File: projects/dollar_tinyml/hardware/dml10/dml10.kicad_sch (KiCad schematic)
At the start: 24 parts, among them J1 Conn_01x03, J2 USB_A, J3 Conn_01x04, U1 CH32V003F4P6, U2 LTC4054ES5-4.2, U3 LIS2DH, U4 LM321

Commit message: dollarml: Some notes on trees and Human Activity Detection
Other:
- note added: "CH32V003A4M6"
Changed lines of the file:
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@@
     (effects (font (size 3 3)) (justify left bottom))
+  )
+  (text "CH32V003A4M6" (at 130.175 70.485 0)
+    (effects (font (size 1.27 1.27)) (justify left bottom))
   )
   (text "Bias" (at 44.45 163.195 0)

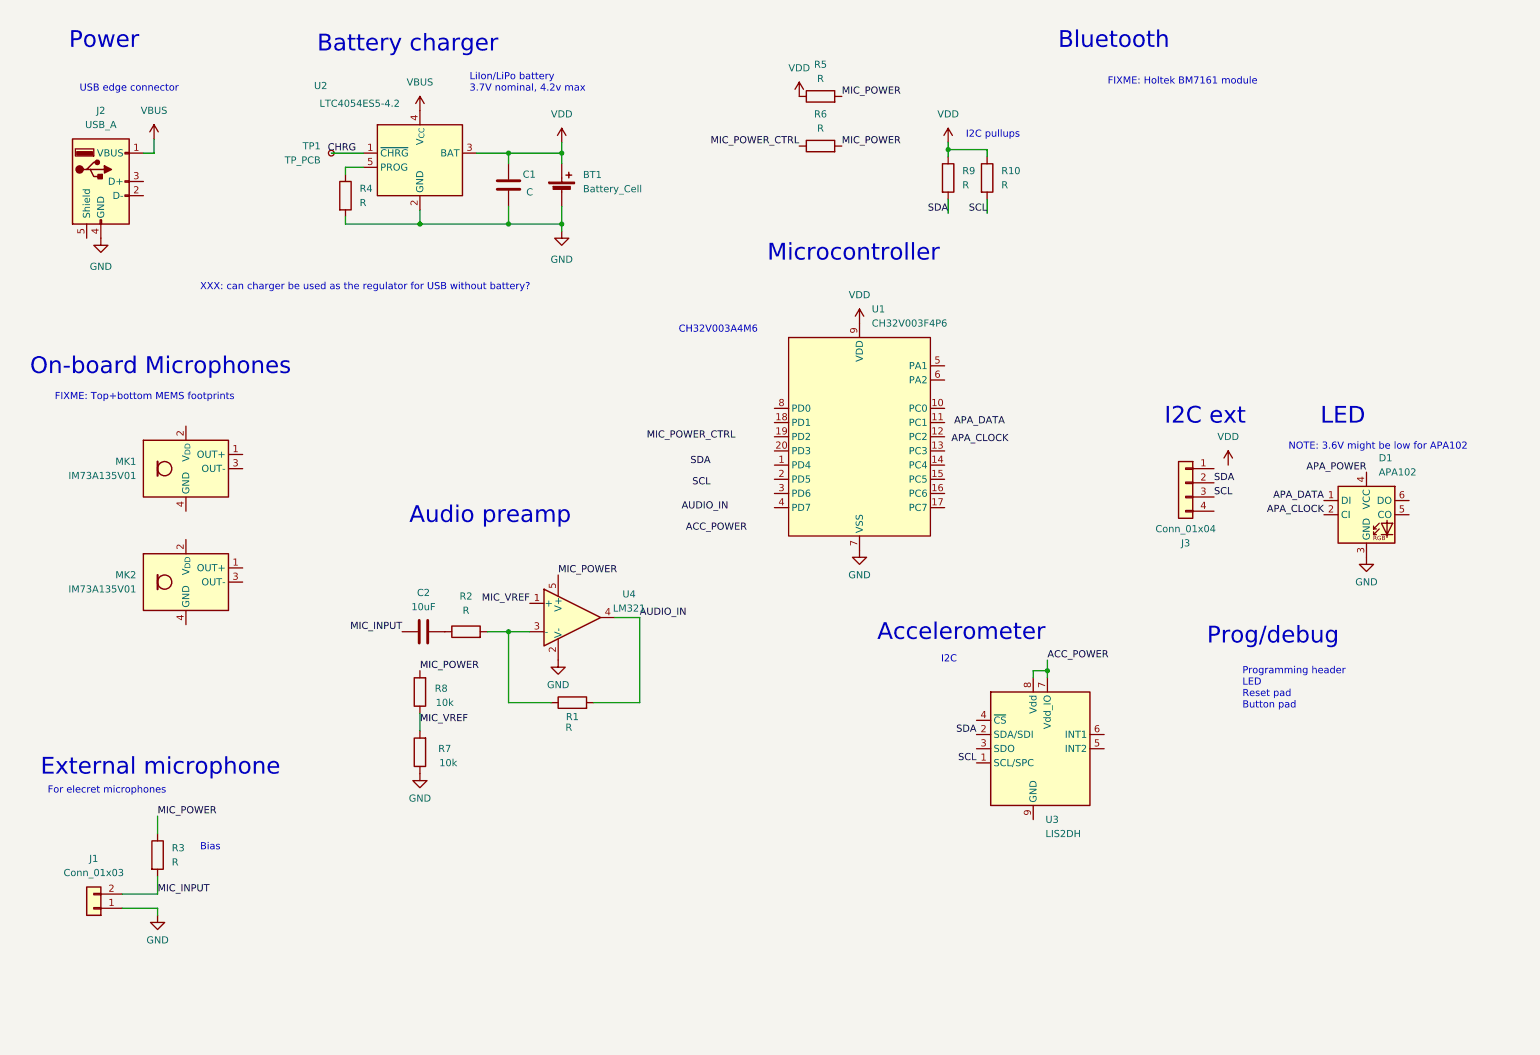
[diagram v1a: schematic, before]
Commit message: dollarml: Schematic and board sketch
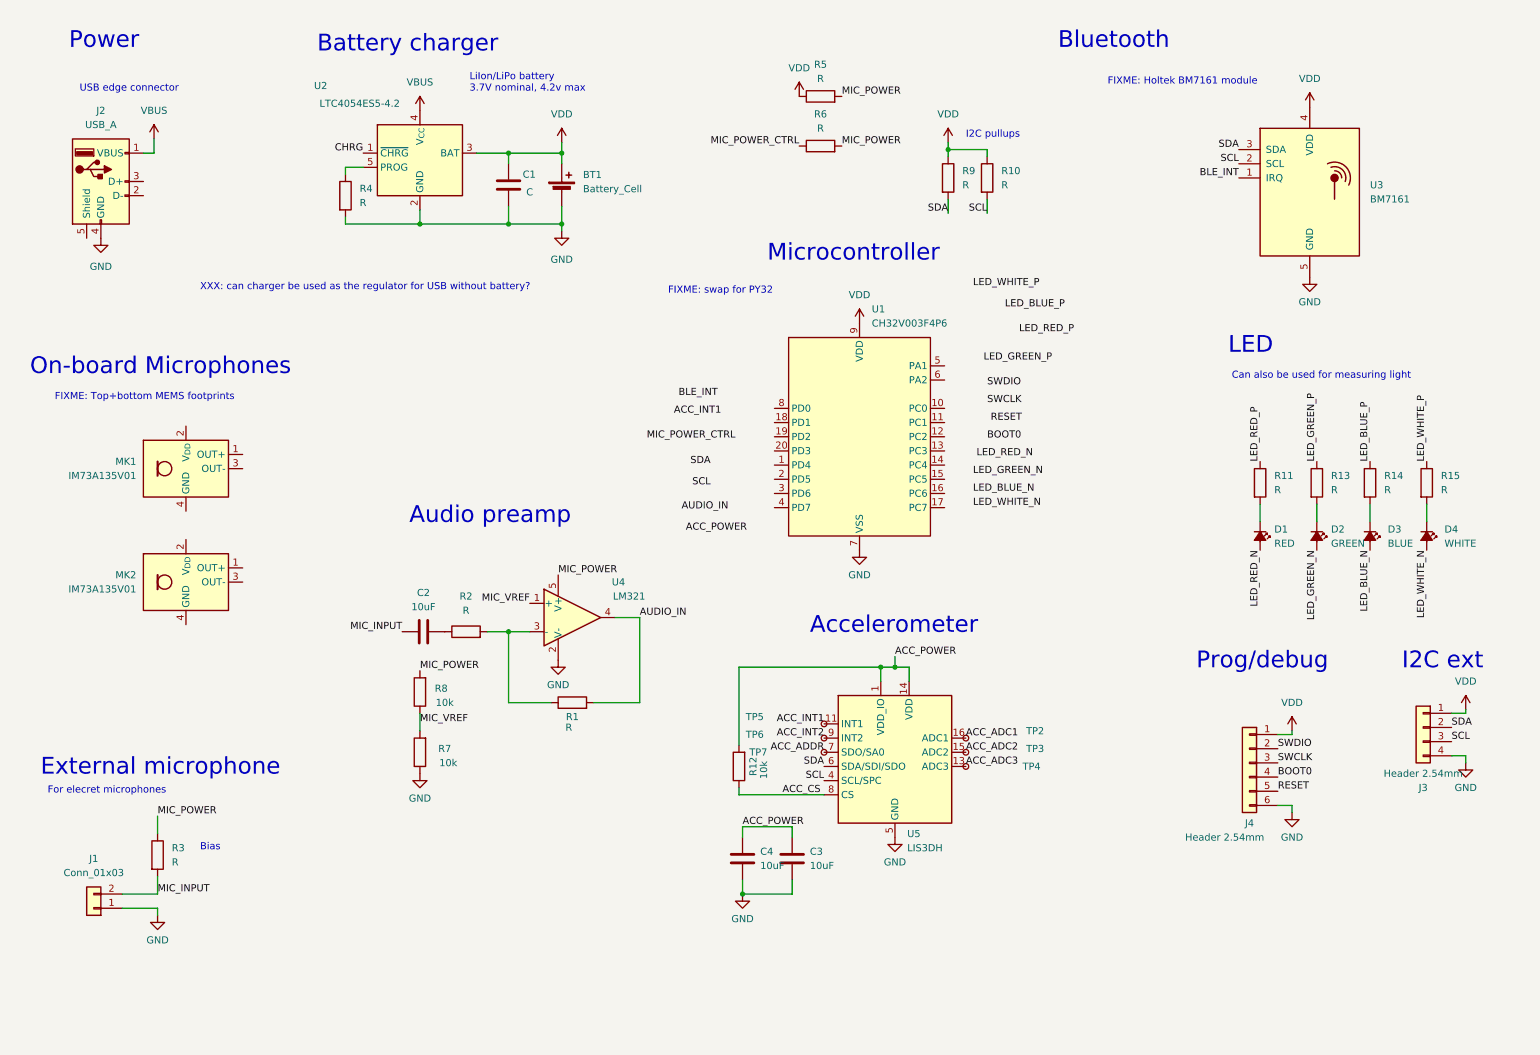
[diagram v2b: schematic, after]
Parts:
- removed D1: APA102, LED_SMD:LED_RGB_5050-6, symbol LED:APA102
- removed TP1: TP_PCB, symbol Connector:TestPoint_Small
- removed U3: LIS2DH, Package_LGA:LGA-14_2x2mm_P0.35mm_LayoutBorder3x4y, symbol Sensor_Motion:LIS2DH
- added C3, C4: 10uF, Capacitor_SMD:C_0603_1608Metric, symbol Device:C
- added D1: RED, LED_SMD:LED_0603_1608Metric, symbol Device:LED_Small_Filled
- added D2: GREEN, LED_SMD:LED_0603_1608Metric, symbol Device:LED_Small_Filled
- added D3: BLUE, LED_SMD:LED_0603_1608Metric, symbol Device:LED_Small_Filled
- added D4: WHITE, LED_SMD:LED_0603_1608Metric, symbol Device:LED_Small_Filled
- added J4: Header 2.54mm, Connector_PinHeader_2.54mm:PinHeader_1x06_P2.54mm_Vertical, symbol Connector_Generic:Conn_01x06
- added R11, R13, R14, R15: R, Resistor_SMD:R_0603_1608Metric, symbol Device:R
- added R12: 10k, Resistor_SMD:R_0603_1608Metric, symbol Device:R
- added TP2, TP3, TP4, TP5, TP6, TP7: TP_PCB, TestPoint:TestPoint_Pad_D1.0mm, symbol Connector:TestPoint_Small
- added U3: BM7161, RF_Module:nRF24L01_Breakout, symbol dml10:BM7161
- added U5: LIS3DH, Package_LGA:LGA-16_3x3mm_P0.5mm_LayoutBorder3x5y, symbol Sensor_Motion:LIS3DH
- BT1, J1: footprint (none) -> Connector_PinHeader_2.54mm:PinHeader_1x02_P2.54mm_Vertical
- C1, C2: footprint (none) -> Capacitor_SMD:C_0603_1608Metric
- J2: footprint (none) -> Connector_USB:USB_A_Receptacle_GCT_USB1046
- J3: value Conn_01x04 -> Header 2.54mm; footprint (none) -> Connector_PinHeader_2.54mm:PinHeader_1x04_P2.54mm_Vertical
- R1, R10, R2, R3, R4, R5, R6, R7, R8, R9: footprint (none) -> Resistor_SMD:R_0603_1608Metric
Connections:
- net ACC_POWER: now also C3.1, C4.1, R12.2, U5.1 (VDD_IO), U5.14 (VDD)
- net GND: now also J3.4 (Pin_4), C3.2, C4.2, J4.6 (Pin_6), U3.5 (GND), U5.10 (GND), U5.12 (GND), U5.5 (GND)
- net SCL: now also U3.2 (SCL), U5.4 (SCL/SPC)
- net SDA: now also U3.3 (SDA), U5.6 (SDA/SDI/SDO)
- net VDD: now also J3.1 (Pin_1), J4.1 (Pin_1), U3.4 (VDD)
- new net: D2.1 (K), R13.2
- new net: D4.1 (K), R15.2
- new net: D3.1 (K), R14.2
- new net: D1.1 (K), R11.2
- new net ACC_ADC1: TP2.1, U5.16 (ADC1)
- new net ACC_ADC2: TP3.1, U5.15 (ADC2)
- new net ACC_ADC3: TP4.1, U5.13 (ADC3)
- new net ACC_ADDR: TP7.1, U5.7 (SDO/SA0)
- new net ACC_CS: R12.1, U5.8 (CS)
- new net ACC_INT1: TP5.1, U5.11 (INT1)
- new net ACC_INT2: TP6.1, U5.9 (INT2)
- new net BLE_INT: U3.1 (IRQ)
- new net BOOT0: J4.4 (Pin_4)
- new net LED_BLUE_N: D3.2 (A)
- new net LED_BLUE_P: R14.1
- new net LED_GREEN_N: D2.2 (A)
- new net LED_GREEN_P: R13.1
- new net LED_RED_N: D1.2 (A)
- new net LED_RED_P: R11.1
- new net LED_WHITE_N: D4.2 (A)
- new net LED_WHITE_P: R15.1
- new net RESET: J4.5 (Pin_5)
- new net SWCLK: J4.3 (Pin_3)
- new net SWDIO: J4.2 (Pin_2)
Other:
- note added: "Can also be used for measuring light"
- note added: "FIXME: swap for PY32"
- note removed: "CH32V003A4M6"
- note removed: "I2C"
- note removed: "NOTE: 3.6V might be low for APA102"
- note removed: "Programming header LED Reset pad Button pad"
- moved on the sheet: J3

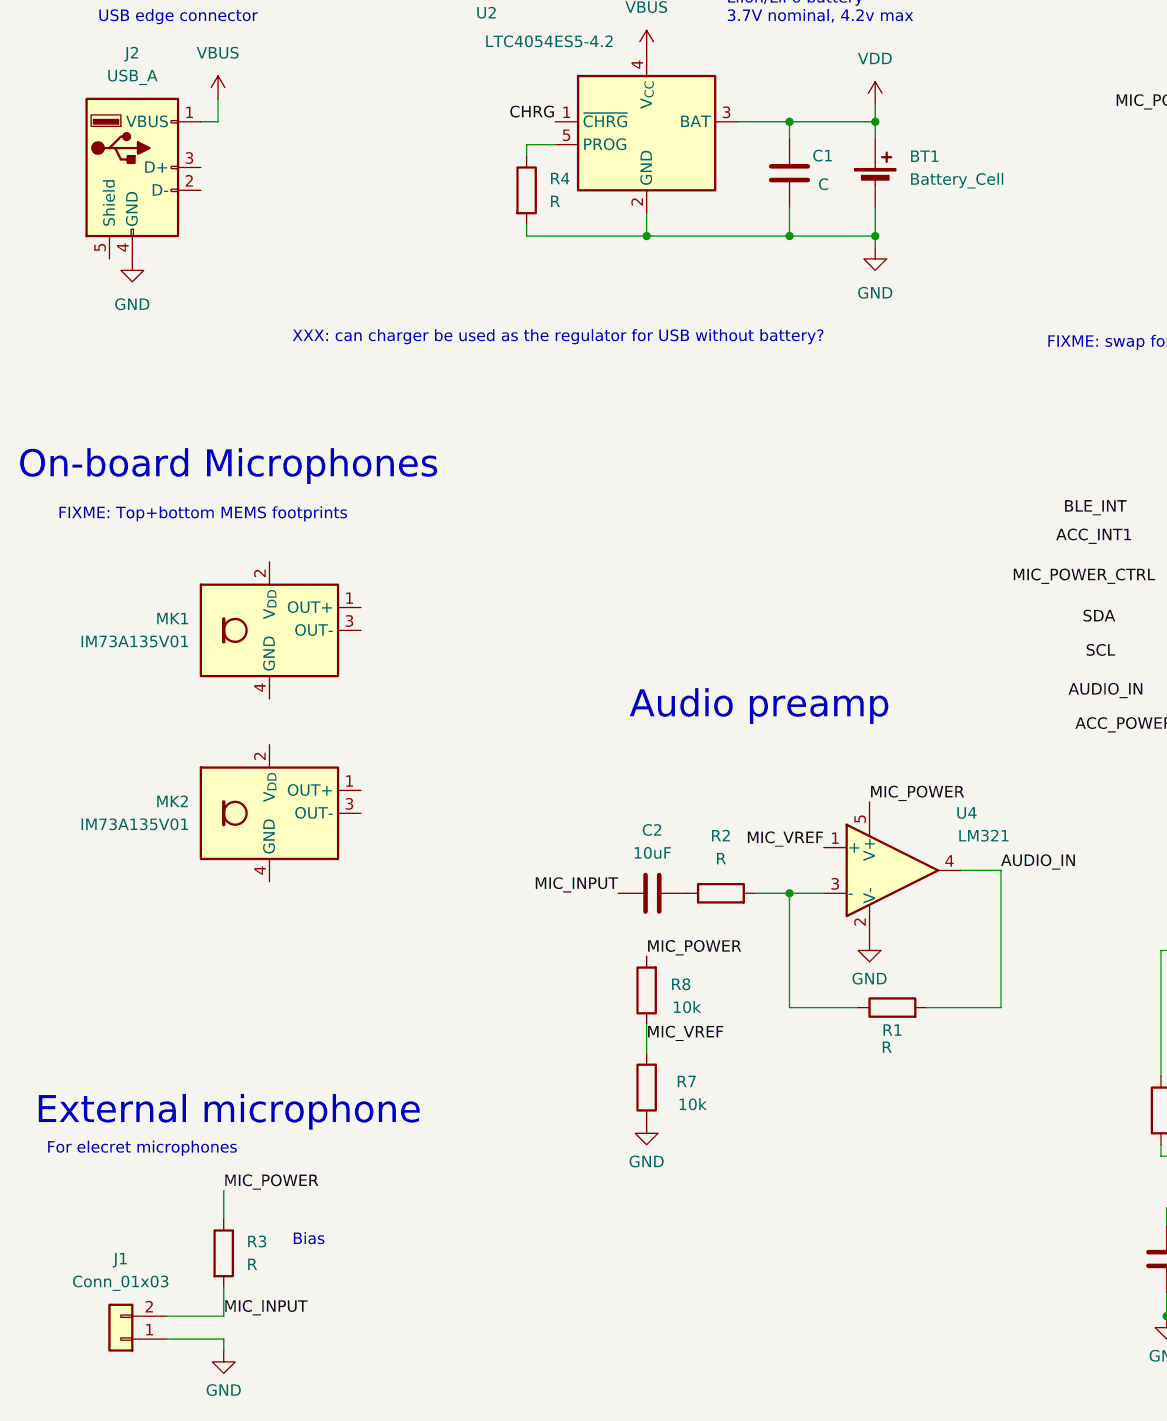
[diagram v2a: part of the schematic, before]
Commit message: dollarml: Rought footprints and layout in place
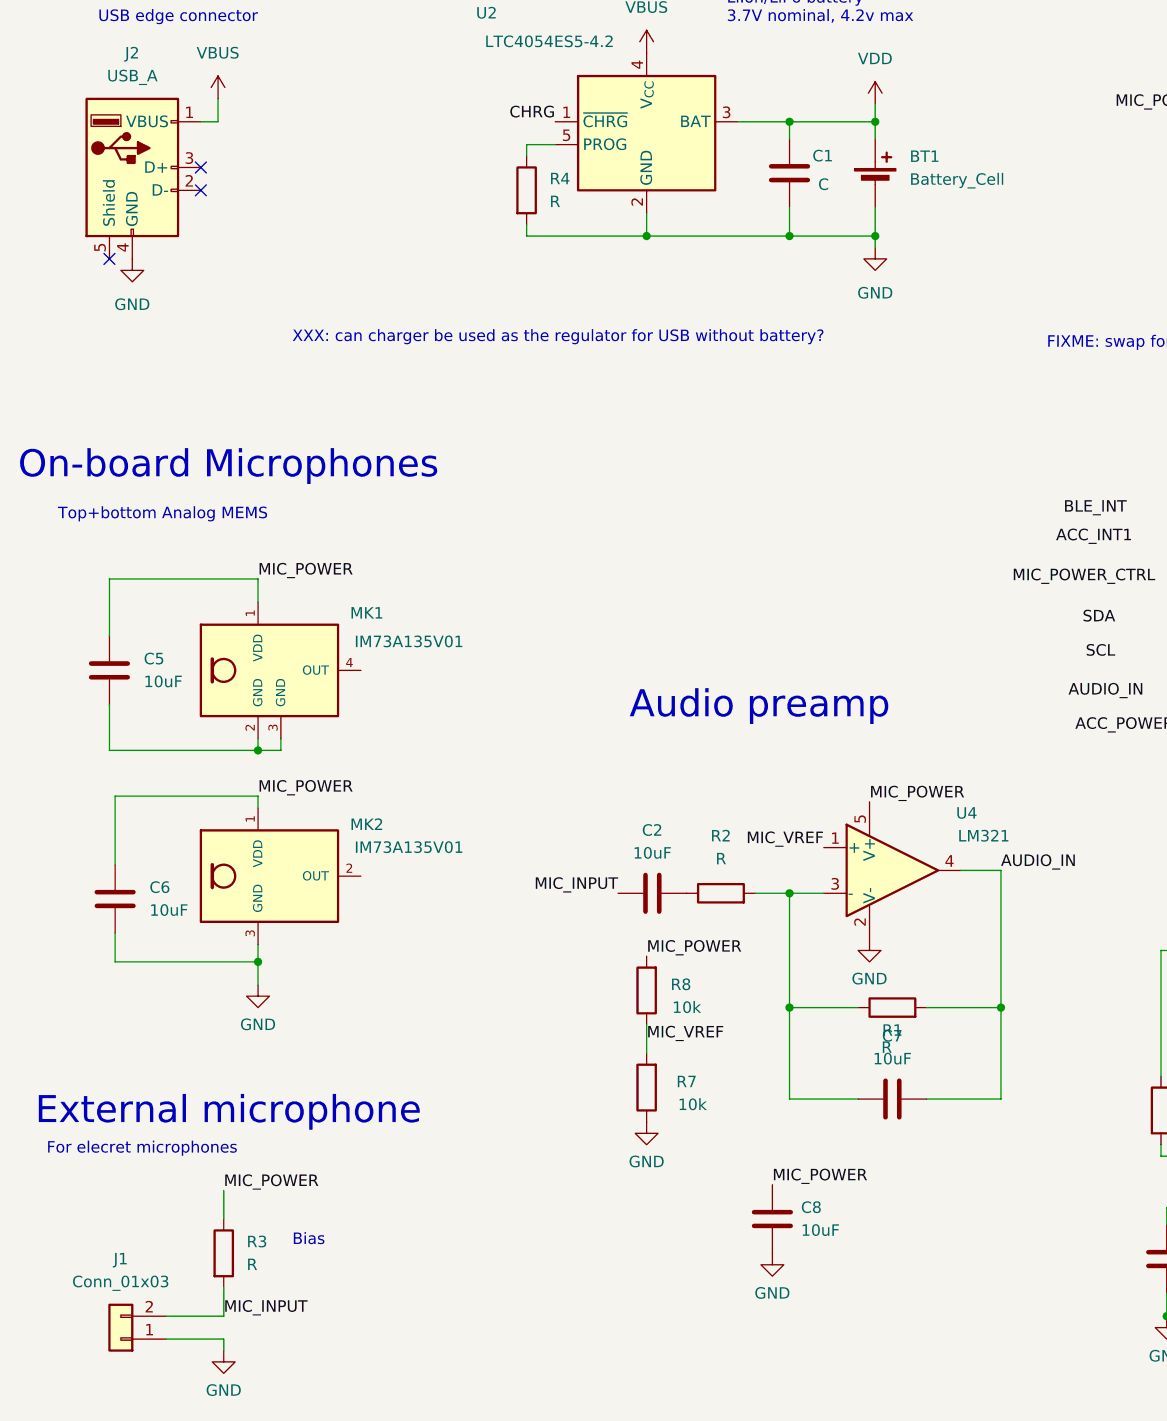
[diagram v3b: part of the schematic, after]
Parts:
- added C5, C6, C7, C8: 10uF, Capacitor_SMD:C_0603_1608Metric, symbol Device:C
- J2: footprint Connector_USB:USB_A_Receptacle_GCT_USB1046 -> dml10:EdgeUSBTypeA
- MK1: footprint Sensor_Audio:Infineon_PG-LLGA-5-2 -> dml10:XDCR_CMM-2718AT-42308-TR; symbol Sensor_Audio:IM73A135V01 -> dml10:AnalogMemsMic4pinTop; MANUFACTURER (none) -> CUI Inc; STANDARD (none) -> Manufacturer Recommendations
- MK2: footprint Sensor_Audio:Infineon_PG-LLGA-5-2 -> dml10:XDCR_CMM-2718AB-383161-TR; symbol Sensor_Audio:IM73A135V01 -> dml10:AnalogMemsMic3pinBottom; MANUFACTURER (none) -> CUI Inc; STANDARD (none) -> Manufacturer Recommendations
- U3: footprint RF_Module:nRF24L01_Breakout -> dml10:BM7161
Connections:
- net AUDIO_IN: now also C7.2
- net GND: now also MK2.3 (GND), C6.2, C8.1
- net MIC_POWER: now also MK1.1 (VDD), MK2.1 (VDD), C5.1, C6.1, C8.2
- net at MK1.2 (GND): now also MK1.3 (GND), C5.2
- net at MK1.4 (OUT): no longer MK1.5 (GND)
- net at R1.1, R2.2, U4.3 (-): now also C7.1
- no-connect marks 0 -> 3
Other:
- note added: "Top+bottom Analog MEMS"
- note removed: "FIXME: Top+bottom MEMS footprints"
- moved on the sheet: MK1
